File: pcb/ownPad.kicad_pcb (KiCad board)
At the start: 2 copper layers, 87 x 45 mm, 15 parts, among them J1 OLED_DISPLAY, SW1 RotaryEncoder_Switch, SW2 SW_Push, SW3 SW_Push, SW4 SW_Push, SW5 SW_Push, SW6 RotaryEncoder_Switch, U1 MOUDLE-SEEEDUINO-XIAO

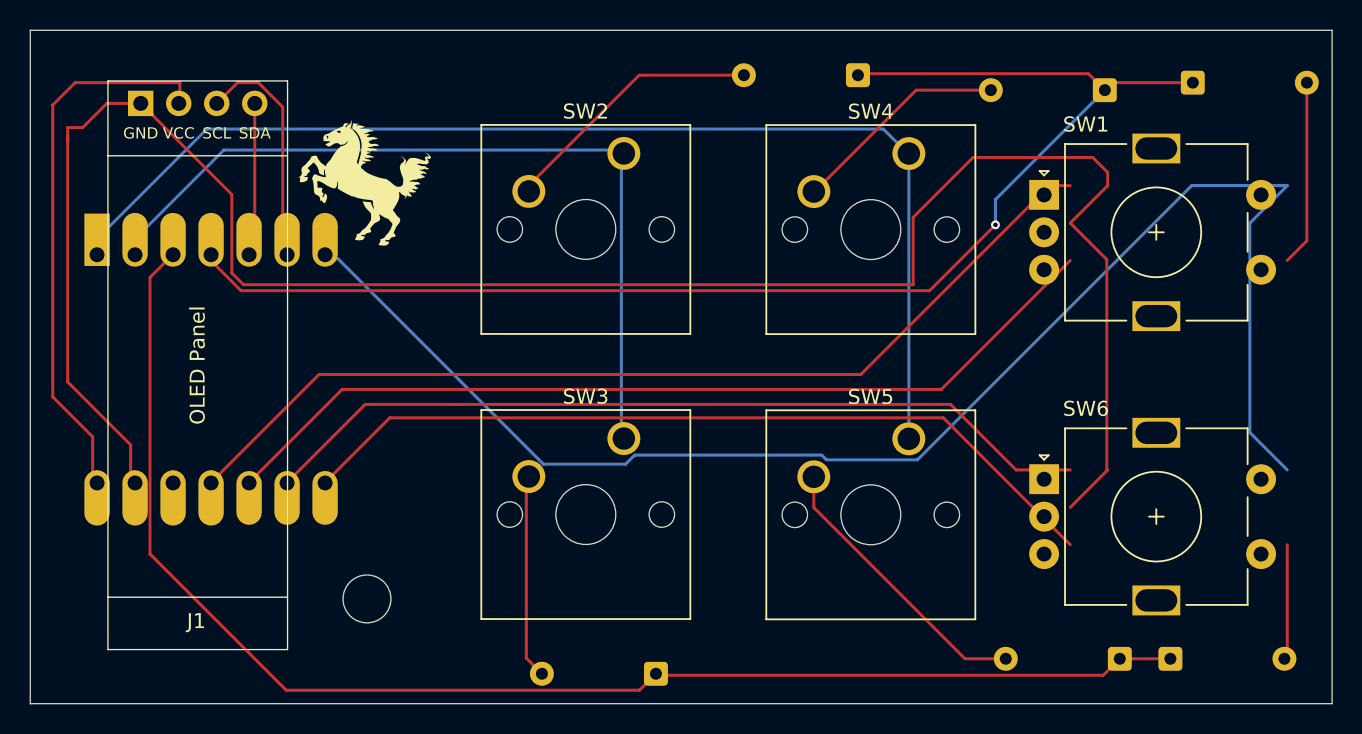
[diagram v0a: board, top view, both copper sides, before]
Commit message: fixed unconnected traces on pcb
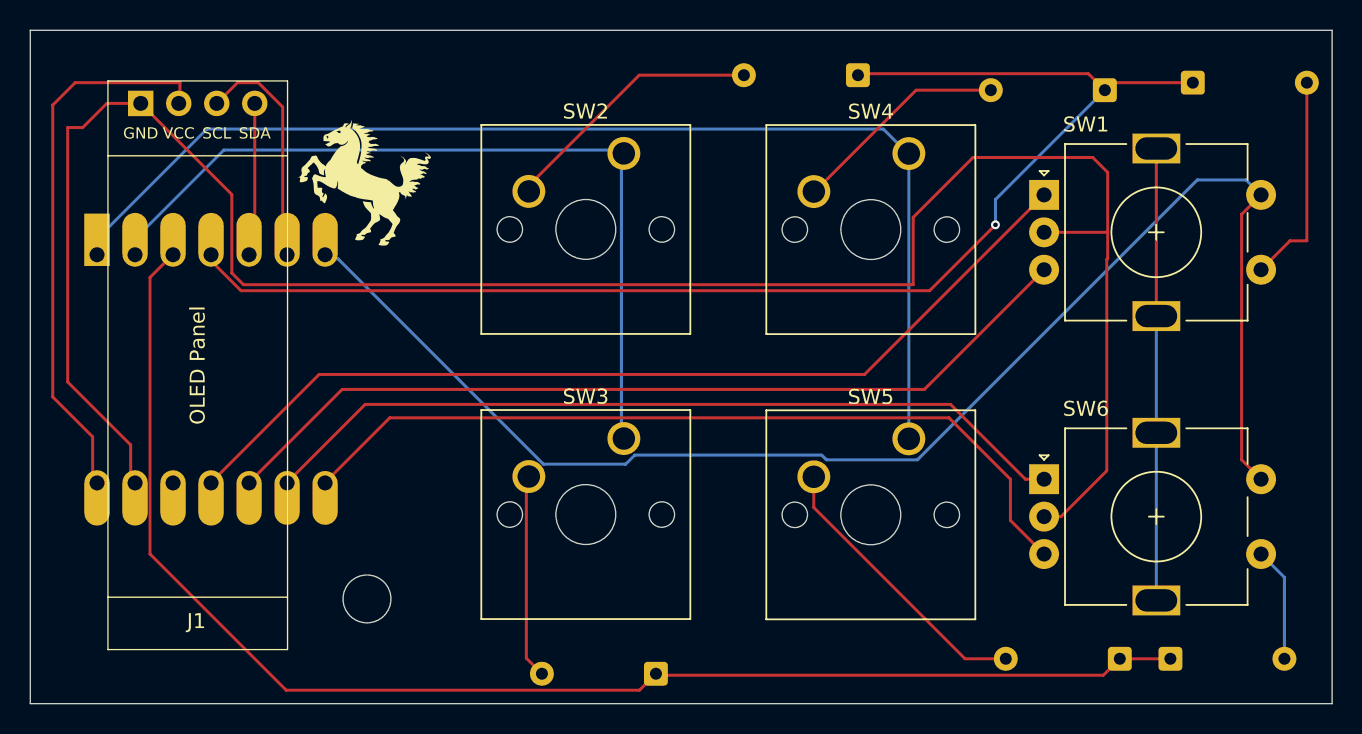
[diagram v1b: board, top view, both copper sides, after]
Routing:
- net (no net): track 0.00 -> 30.2 mm
- net GND: track 136.6 -> 140.3 mm
- net EC11A: track 66.2 -> 64.0 mm
- net COL2: track 99.3 -> 97.2 mm
- net EC11B: track 61.4 -> 59.4 mm
- net Net-(D2-A): track 12.4 -> 14.4 mm
- net EC22A: track 57.2 -> 55.2 mm
- net ROW0: track 91.2 -> 90.6 mm

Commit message: removed errors in pcb design
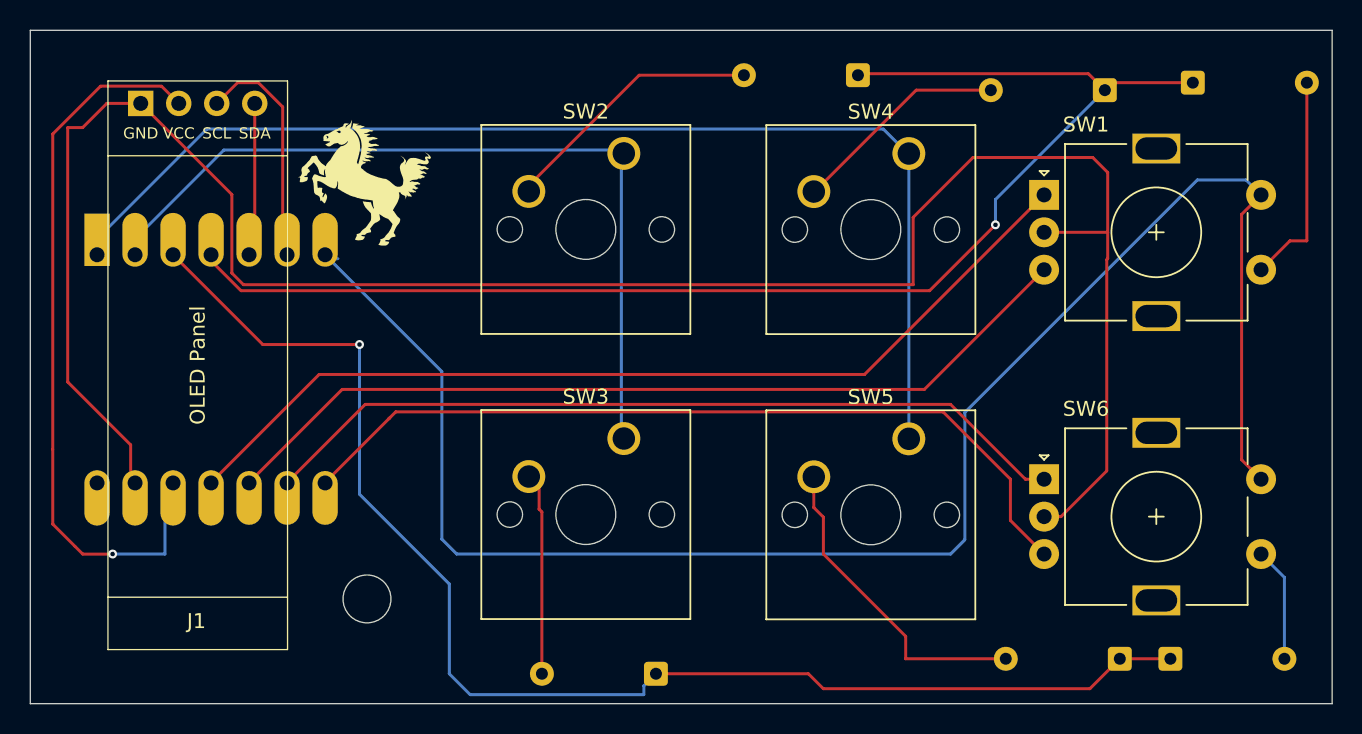
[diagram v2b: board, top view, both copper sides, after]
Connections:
- J1 pad 2: VCC -> Net-(J1-Pin_2)
- U1 pad 12: unconnected-(U1-3V3-Pad12) -> Net-(J1-Pin_2)
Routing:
- net Net-(J1-Pin_2): track 0.00 -> 50.9 mm, vias 0 -> 1
- net VCC: track 37.2 -> 0.00 mm
- net (no net): track 30.2 -> 0.00 mm
- net COL2: track 97.2 -> 114.4 mm
- net ROW1: track 93.2 -> 90.7 mm, vias 0 -> 1
- net Net-(D6-A): track 19.1 -> 21.4 mm
